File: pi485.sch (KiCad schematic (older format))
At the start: 25 parts, among them J1 RS485, P1 Rasperry Pi, P2 PWR, P3 Term, Q1 2N2222, Q2 2N2222, Q3 2N2222, U1 NE555, U2 MAX485

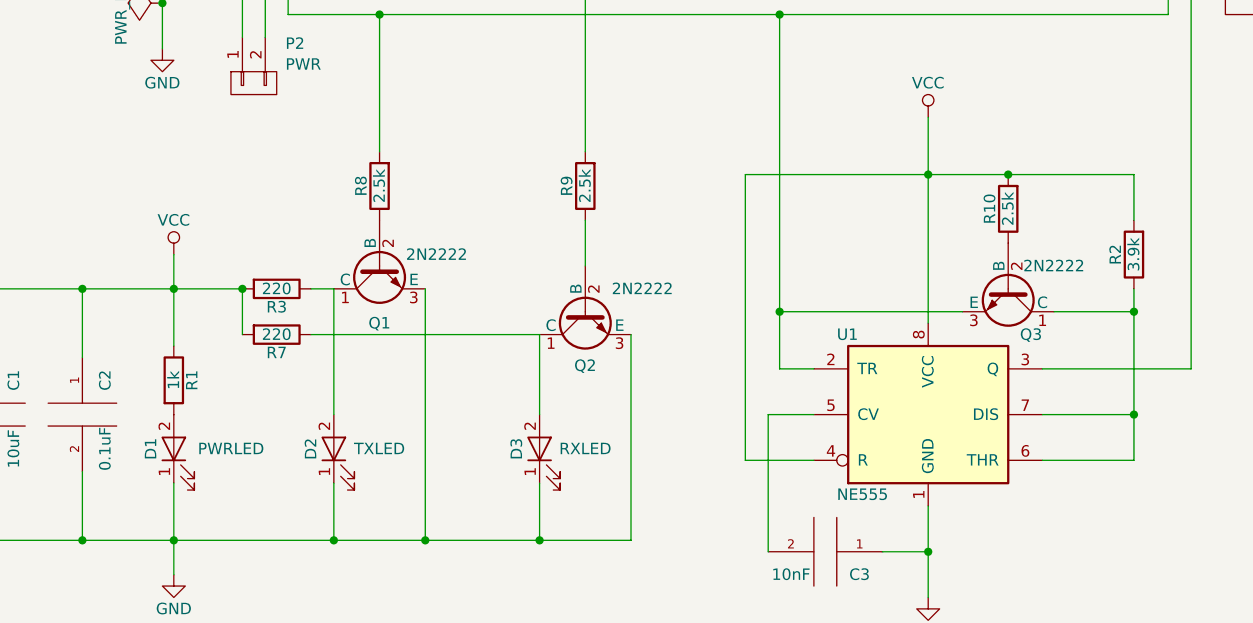
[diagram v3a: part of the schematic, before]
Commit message: Resistor / LED adjustments, BAT43 restoration (digi-key order placed). Footprint updates.
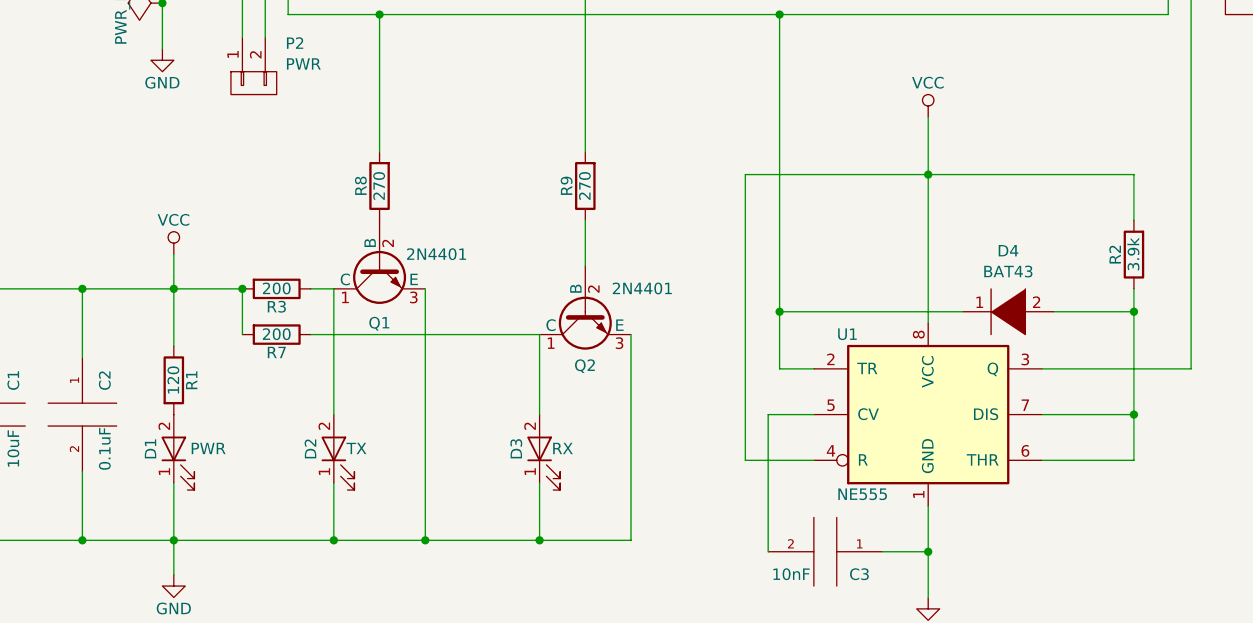
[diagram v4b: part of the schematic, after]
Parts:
- removed Q3: 2N2222, TO_SOT_Packages_THT:TO-92_Inline_Wide, symbol BC413
- removed R10: 2.5k, Resistors_THT:Resistor_Horizontal_RM7mm, symbol R
- added D4: BAT43, Diodes_THT:Diode_DO-35_SOD27_Horizontal_RM10, symbol DIODE
- C1: footprint Capacitors_THT:C_Rect_L7_W2.5_P5 -> Capacitors_THT:C_Radial_D5_L11_P2
- D1: value PWRLED -> PWR; footprint LEDs:LED-5MM -> LEDs:LED-3MM
- D2: value TXLED -> TX; footprint LEDs:LED-5MM -> LEDs:LED-3MM
- D3: value RXLED -> RX; footprint LEDs:LED-5MM -> LEDs:LED-3MM
- Q1, Q2: value 2N2222 -> 2N4401
- R1: value 1k -> 120
- R3, R7: value 220 -> 200
- R8, R9: value 2.5k -> 270
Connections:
- net (TXDO)_GPIO14: now also D4.1 (K)
- net at R2.1, U1.6 (THR), U1.7 (DIS): now also D4.2 (A)
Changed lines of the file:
@@
 Comp "Bryan Varner"
 Comment1 ""
-Comment2 ""
+Comment2 "Size resistor values R1, R3, and R7 appropriately for your LED choices."
 Comment3 "Implements half-duplex with TX latched RE/DE"
 Comment4 "Raspberry Pi / Arduino UART to RS485"
 $EndDescr
 $Comp
-L GND #PWR01
+L GND #PWR2
 U 1 1 586E82C6
 P 2150 3250
-F 0 "#PWR01" H 2150 3000 50  0001 C CNN
+F 0 "#PWR2" H 2150 3000 50  0001 C CNN
 F 1 "GND" H 2150 3100 50  0000 C CNN
 F 2 "" H 2150 3250 50  0000 C CNN
@@
 $EndComp
 $Comp
-L PWR_FLAG #FLG02
+L PWR_FLAG #FLG1
 U 1 1 586E8329
 P 2150 2150
-F 0 "#FLG02" H 2150 2245 50  0001 C CNN
+F 0 "#FLG1" H 2150 2245 50  0001 C CNN
 F 1 "PWR_FLAG" H 2150 2330 50  0000 C CNN
 F 2 "" H 2150 2150 50  0000 C CNN
@@
 $EndComp
 $Comp
-L PWR_FLAG #FLG03
+L PWR_FLAG #FLG2
 U 1 1 586E8340
 P 2150 3050
-F 0 "#FLG03" H 2150 3145 50  0001 C CNN
+F 0 "#FLG2" H 2150 3145 50  0001 C CNN
 F 1 "PWR_FLAG" H 2150 3230 50  0000 C CNN
 F 2 "" H 2150 3050 50  0000 C CNN
@@
 $EndComp
 $Comp
-L VCC #PWR04
+L VCC #PWR1
 U 1 1 586E83C6
 P 2150 1850
-F 0 "#PWR04" H 2150 1700 50  0001 C CNN
+F 0 "#PWR1" H 2150 1700 50  0001 C CNN
 F 1 "VCC" H 2150 2000 50  0000 C CNN
 F 2 "" H 2150 1850 50  0000 C CNN
@@
 $EndComp
 $Comp
-L VCC #PWR05
+L VCC #PWR3
 U 1 1 586E8496
 P 2200 4150
-F 0 "#PWR05" H 2200 4000 50  0001 C CNN
+F 0 "#PWR3" H 2200 4000 50  0001 C CNN
 F 1 "VCC" H 2200 4300 50  0000 C CNN
 F 2 "" H 2200 4150 50  0000 C CNN
@@
 $EndComp
 $Comp
-L GND #PWR06
+L GND #PWR4
 U 1 1 586E84AD
 P 2200 5550
-F 0 "#PWR06" H 2200 5300 50  0001 C CNN
+F 0 "#PWR4" H 2200 5300 50  0001 C CNN
 F 1 "GND" H 2200 5400 50  0000 C CNN
 F 2 "" H 2200 5550 50  0000 C CNN
@@
 P 2200 4700
 F 0 "R1" V 2280 4700 50  0000 C CNN
-F 1 "1k" V 2200 4700 50  0000 C CNN
+F 1 "120" V 2200 4700 50  0000 C CNN
 F 2 "Resistors_THT:Resistor_Horizontal_RM7mm" V 2350 4000 50  0001 C CNN
 F 3 "" H 2200 4700 50  0000 C CNN
@@
 P 2200 5000
 F 0 "D1" H 2200 5100 50  0000 C CNN
-F 1 "PWRLED" V 2200 4750 50  0000 C CNN
-F 2 "LEDs:LED-5MM" H 2150 4800 50  0001 C CNN
+F 1 "PWR" V 2200 4850 50  0000 C CNN
+F 2 "LEDs:LED-3MM" H 2150 4800 50  0001 C CNN
 F 3 "" H 2200 5000 50  0000 C CNN
 	1    2200 5000
@@
 $EndComp
 $Comp
-L GND #PWR07
+L GND #PWR6
 U 1 1 586E98F0
 P 5500 5650
-F 0 "#PWR07" H 5500 5400 50  0001 C CNN
+F 0 "#PWR6" H 5500 5400 50  0001 C CNN
 F 1 "GND" H 5500 5500 50  0000 C CNN
 F 2 "" H 5500 5650 50  0000 C CNN
@@
 $EndComp
 $Comp
-L VCC #PWR08
+L VCC #PWR5
 U 1 1 586E9922
 P 5500 3550
-F 0 "#PWR08" H 5500 3400 50  0001 C CNN
+F 0 "#PWR5" H 5500 3400 50  0001 C CNN
 F 1 "VCC" H 5500 3700 50  0000 C CNN
 F 2 "" H 5500 3550 50  0000 C CNN
@@
 $EndComp
 $Comp
-L GND #PWR09
+L GND #PWR8
 U 1 1 586EB44F
 P 7100 3500
-F 0 "#PWR09" H 7100 3250 50  0001 C CNN
+F 0 "#PWR8" H 7100 3250 50  0001 C CNN
 F 1 "GND" H 7100 3350 50  0000 C CNN
 F 2 "" H 7100 3500 50  0000 C CNN
@@
 $EndComp
 $Comp
-L VCC #PWR010
+L VCC #PWR7
 U 1 1 586EB484
 P 7100 1650
-F 0 "#PWR010" H 7100 1500 50  0001 C CNN
+F 0 "#PWR7" H 7100 1500 50  0001 C CNN
 F 1 "VCC" H 7100 1800 50  0000 C CNN
 F 2 "" H 7100 1650 50  0000 C CNN
@@
 GND
 $Comp
-L GND #PWR011
+L GND #PWR9
 U 1 1 586F0172
 P 8250 1900
-F 0 "#PWR011" H 8250 1650 50  0001 C CNN
+F 0 "#PWR9" H 8250 1650 50  0001 C CNN
 F 1 "GND" H 8250 1750 50  0000 C CNN
 F 2 "" H 8250 1900 50  0000 C CNN
@@
 $EndComp
 $Comp
-L VCC #PWR012
+L VCC #PWR10
 U 1 1 586F01EA
 P 8250 3300
-F 0 "#PWR012" H 8250 3150 50  0001 C CNN
+F 0 "#PWR10" H 8250 3150 50  0001 C CNN
 F 1 "VCC" H 8250 3450 50  0000 C CNN
 F 2 "" H 8250 3300 50  0000 C CNN
@@
 $EndComp
 $Comp
-L R R10
-U 1 1 5876AB08
-P 5850 3950
-F 0 "R10" V 5930 3950 50  0000 C CNN
-F 1 "2.5k" V 5850 3950 50  0000 C CNN
-F 2 "Resistors_THT:Resistor_Horizontal_RM7mm" H 4950 3950 50  0001 C CNN
-F 3 "" H 5850 3950 50  0000 C CNN
-	1    5850 3950
-	-1   0    0    1
-$EndComp
-$Comp
-L BC413 Q3
-U 1 1 5876AECB
-P 5850 4300
-F 0 "Q3" V 6050 4400 50  0000 C CNN
-F 1 "2N2222" V 5750 4500 50  0000 C CNN
-F 2 "TO_SOT_Packages_THT:TO-92_Inline_Wide" V 6268 4300 50  0001 C CIN
-F 3 "" H 5850 4300 50  0000 L CNN
-	1    5850 4300
-	0    1    1    0
-$EndComp
-$Comp
 L BC413 Q1
 U 1 1 5876C3F8
 P 3100 4200
 F 0 "Q1" V 3350 4200 50  0000 C CNN
-F 1 "2N2222" V 3050 3950 50  0000 C CNN
+F 1 "2N4401" V 3050 3950 50  0000 C CNN
 F 2 "TO_SOT_Packages_THT:TO-92_Inline_Wide" V 3518 4200 50  0001 C CIN
 F 3 "" H 3100 4200 50  0000 L CNN
@@
 P 4000 4400
 F 0 "Q2" V 4236 4400 50  0000 C CNN
-F 1 "2N2222" V 3900 4150 50  0000 C CNN
+F 1 "2N4401" V 3900 4150 50  0000 C CNN
 F 2 "TO_SOT_Packages_THT:TO-92_Inline_Wide" V 4418 4400 50  0001 C CIN
 F 3 "" H 4000 4400 50  0000 L CNN
@@
 P 2900 5000
 F 0 "D2" H 2900 5100 50  0000 C CNN
-F 1 "TXLED" V 2900 4800 50  0000 C CNN
-F 2 "LEDs:LED-5MM" H 2850 4800 50  0001 C CNN
+F 1 "TX" V 2900 4900 50  0000 C CNN
+F 2 "LEDs:LED-3MM" H 2850 4800 50  0001 C CNN
 F 3 "" H 2900 5000 50  0000 C CNN
 	1    2900 5000
@@
 P 3800 5000
 F 0 "D3" H 3800 5100 50  0000 C CNN
-F 1 "RXLED" V 3800 4800 50  0000 C CNN
-F 2 "LEDs:LED-5MM" H 3750 4800 50  0001 C CNN
+F 1 "RX" V 3800 4900 50  0000 C CNN
+F 2 "LEDs:LED-3MM" H 3750 4800 50  0001 C CNN
 F 3 "" H 3800 5000 50  0000 C CNN
 	1    3800 5000
@@
 P 2650 4500
 F 0 "R7" V 2730 4500 50  0000 C CNN
-F 1 "220" V 2650 4500 50  0000 C CNN
+F 1 "200" V 2650 4500 50  0000 C CNN
 F 2 "Resistors_THT:Resistor_Horizontal_RM7mm" V 2800 3800 50  0001 C CNN
 F 3 "" H 2650 4500 50  0000 C CNN
@@
 P 2650 4300
 F 0 "R3" V 2730 4300 50  0000 C CNN
-F 1 "220" V 2650 4300 50  0000 C CNN
+F 1 "200" V 2650 4300 50  0000 C CNN
 F 2 "Resistors_THT:Resistor_Horizontal_RM7mm" V 2800 3600 50  0001 C CNN
 F 3 "" H 2650 4300 50  0000 C CNN
@@
 P 3100 3850
 F 0 "R8" V 3180 3850 50  0000 C CNN
-F 1 "2.5k" V 3100 3850 50  0000 C CNN
+F 1 "270" V 3100 3850 50  0000 C CNN
 F 2 "Resistors_THT:Resistor_Horizontal_RM15mm" V 3250 3150 50  0001 C CNN
 F 3 "" H 3100 3850 50  0000 C CNN
@@
 P 4000 3850
 F 0 "R9" V 4080 3850 50  0000 C CNN
-F 1 "2.5k" V 4000 3850 50  0000 C CNN
+F 1 "270" V 4000 3850 50  0000 C CNN
 F 2 "Resistors_THT:Resistor_Horizontal_RM7mm" V 4150 3150 50  0001 C CNN
 F 3 "" H 4000 3850 50  0000 C CNN
@@
 F 0 "C1" V 1500 5000 50  0000 C CNN
 F 1 "10uF" V 1500 4700 50  0000 C CNN
-F 2 "Capacitors_THT:C_Rect_L7_W2.5_P5" V 1600 4550 50  0001 C CNN
+F 2 "Capacitors_THT:C_Radial_D5_L11_P2" V 1600 4550 50  0001 C CNN
 F 3 "" H 1400 4850 50  0000 C CNN
 	1    1400 4850
@@
 	1800 4600 1800 4300
 Connection ~ 1800 4300
-Connection ~ 5850 3800
 Wire Wire Line
 	6050 4400 6400 4400
+$Comp
+L DIODE D4
+U 1 1 5879650D
+P 5850 4400
+F 0 "D4" H 5850 4665 50  0000 C CNN
+F 1 "BAT43" H 5850 4574 50  0000 C CNN
+F 2 "Diodes_THT:Diode_DO-35_SOD27_Horizontal_RM10" H 5850 4573 50  0001 C CNN
+F 3 "" H 5850 4400 50  0000 C CNN
+	1    5850 4400
+	1    0    0    -1
+$EndComp
 $EndSCHEMATC

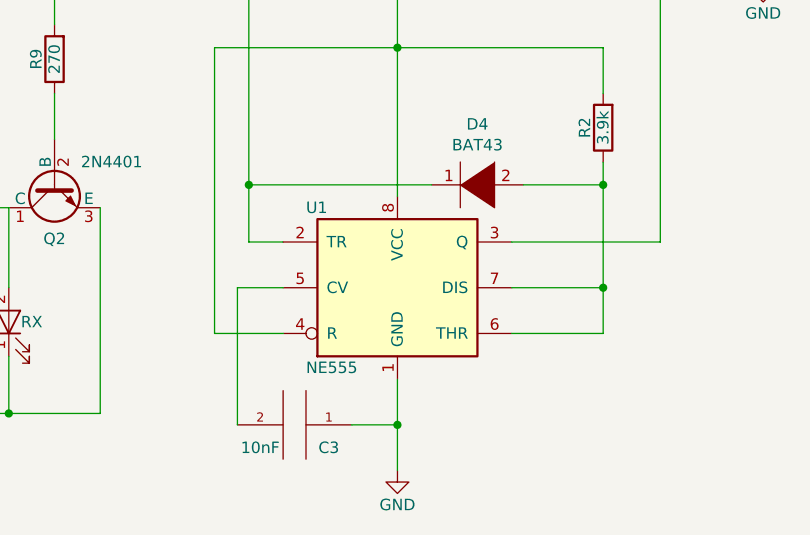
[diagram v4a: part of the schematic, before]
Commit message: * Rotated board 90 degrees. * Major update to footprints. Resistors are 10mm, LEDs are 3mm. * Manually re-routed / cleaned up traces & positiiong of quite a few things. * This could be pulled so much tighter, but to keep it 'simple soldering' I'm deliberately keeping big honkin traces with lots of clearance. * Fixed a major issue where I had accidentally forgotten the discharge capacitor by deleting the wrong one. The CTRL pin of the 555 should be jumperable to GND to keep the output of the 555 low, regardless of input (latch disable).
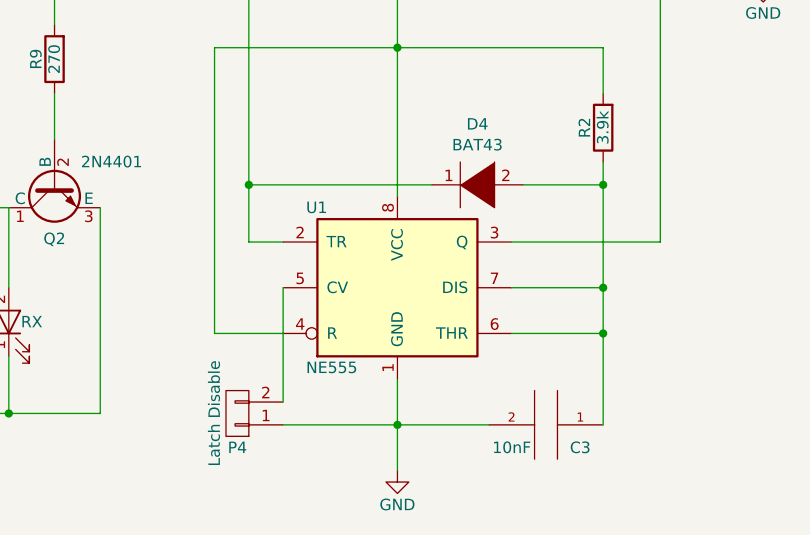
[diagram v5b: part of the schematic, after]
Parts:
- added P4: Latch Disable, Pin_Headers:Pin_Header_Straight_1x02, symbol CONN_01X02
- R1, R3, R4, R5, R6, R7, R9: footprint Resistors_THT:Resistor_Horizontal_RM7mm -> Resistors_THT:Resistor_Horizontal_RM10mm
- R8: footprint Resistors_THT:Resistor_Horizontal_RM15mm -> Resistors_THT:Resistor_Horizontal_RM10mm
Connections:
- net GND: now also C3.2, P4.1 (P1); no longer C3.1
- net at U1.5 (CV): now also P4.2 (P2); no longer C3.2
- net at D4.2 (A), R2.1, U1.6 (THR)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: now also C3.1
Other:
- moved on the sheet: C3
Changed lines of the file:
@@
 Title "Pi485"
 Date "2017-01-12"
-Rev "1.0.1"
+Rev "1.0.4"
 Comp "Bryan Varner"
 Comment1 ""
@@
 $EndDescr
 $Comp
-L GND #PWR2
+L GND #PWR01
 U 1 1 586E82C6
 P 2150 3250
-F 0 "#PWR2" H 2150 3000 50  0001 C CNN
+F 0 "#PWR01" H 2150 3000 50  0001 C CNN
 F 1 "GND" H 2150 3100 50  0000 C CNN
 F 2 "" H 2150 3250 50  0000 C CNN
@@
 $EndComp
 $Comp
-L PWR_FLAG #FLG1
+L PWR_FLAG #FLG02
 U 1 1 586E8329
 P 2150 2150
-F 0 "#FLG1" H 2150 2245 50  0001 C CNN
+F 0 "#FLG02" H 2150 2245 50  0001 C CNN
 F 1 "PWR_FLAG" H 2150 2330 50  0000 C CNN
 F 2 "" H 2150 2150 50  0000 C CNN
@@
 $EndComp
 $Comp
-L PWR_FLAG #FLG2
+L PWR_FLAG #FLG03
 U 1 1 586E8340
 P 2150 3050
-F 0 "#FLG2" H 2150 3145 50  0001 C CNN
+F 0 "#FLG03" H 2150 3145 50  0001 C CNN
 F 1 "PWR_FLAG" H 2150 3230 50  0000 C CNN
 F 2 "" H 2150 3050 50  0000 C CNN
@@
 $EndComp
 $Comp
-L VCC #PWR1
+L VCC #PWR04
 U 1 1 586E83C6
 P 2150 1850
-F 0 "#PWR1" H 2150 1700 50  0001 C CNN
+F 0 "#PWR04" H 2150 1700 50  0001 C CNN
 F 1 "VCC" H 2150 2000 50  0000 C CNN
 F 2 "" H 2150 1850 50  0000 C CNN
@@
 $EndComp
 $Comp
-L VCC #PWR3
+L VCC #PWR05
 U 1 1 586E8496
 P 2200 4150
-F 0 "#PWR3" H 2200 4000 50  0001 C CNN
+F 0 "#PWR05" H 2200 4000 50  0001 C CNN
 F 1 "VCC" H 2200 4300 50  0000 C CNN
 F 2 "" H 2200 4150 50  0000 C CNN
@@
 $EndComp
 $Comp
-L GND #PWR4
+L GND #PWR06
 U 1 1 586E84AD
 P 2200 5550
-F 0 "#PWR4" H 2200 5300 50  0001 C CNN
+F 0 "#PWR06" H 2200 5300 50  0001 C CNN
 F 1 "GND" H 2200 5400 50  0000 C CNN
 F 2 "" H 2200 5550 50  0000 C CNN
@@
 F 0 "R1" V 2280 4700 50  0000 C CNN
 F 1 "120" V 2200 4700 50  0000 C CNN
-F 2 "Resistors_THT:Resistor_Horizontal_RM7mm" V 2350 4000 50  0001 C CNN
+F 2 "Resistors_THT:Resistor_Horizontal_RM10mm" V 2350 4000 50  0001 C CNN
 F 3 "" H 2200 4700 50  0000 C CNN
 	1    2200 4700
@@
 L CAP C3
 U 1 1 586E89BC
-P 5050 5450
-F 0 "C3" V 5150 5600 50  0000 C CNN
-F 1 "10nF" V 5150 5300 50  0000 C CNN
-F 2 "Capacitors_THT:C_Rect_L7_W2.5_P5" V 5250 5150 50  0001 C CNN
-F 3 "" H 5050 5450 50  0000 C CNN
-	1    5050 5450
+P 6150 5450
+F 0 "C3" V 6250 5600 50  0000 C CNN
+F 1 "10nF" V 6250 5300 50  0000 C CNN
+F 2 "Capacitors_THT:C_Rect_L7_W2.5_P5" V 6350 5150 50  0001 C CNN
+F 3 "" H 6150 5450 50  0000 C CNN
+	1    6150 5450
 	0    1    1    0
 $EndComp
 $Comp
-L GND #PWR6
+L GND #PWR07
 U 1 1 586E98F0
 P 5500 5650
-F 0 "#PWR6" H 5500 5400 50  0001 C CNN
+F 0 "#PWR07" H 5500 5400 50  0001 C CNN
 F 1 "GND" H 5500 5500 50  0000 C CNN
 F 2 "" H 5500 5650 50  0000 C CNN
@@
 $EndComp
 $Comp
-L VCC #PWR5
+L VCC #PWR08
 U 1 1 586E9922
 P 5500 3550
-F 0 "#PWR5" H 5500 3400 50  0001 C CNN
+F 0 "#PWR08" H 5500 3400 50  0001 C CNN
 F 1 "VCC" H 5500 3700 50  0000 C CNN
 F 2 "" H 5500 3550 50  0000 C CNN
@@
 $EndComp
 $Comp
-L GND #PWR8
+L GND #PWR09
 U 1 1 586EB44F
 P 7100 3500
-F 0 "#PWR8" H 7100 3250 50  0001 C CNN
+F 0 "#PWR09" H 7100 3250 50  0001 C CNN
 F 1 "GND" H 7100 3350 50  0000 C CNN
 F 2 "" H 7100 3500 50  0000 C CNN
@@
 $EndComp
 $Comp
-L VCC #PWR7
+L VCC #PWR010
 U 1 1 586EB484
 P 7100 1650
-F 0 "#PWR7" H 7100 1500 50  0001 C CNN
+F 0 "#PWR010" H 7100 1500 50  0001 C CNN
 F 1 "VCC" H 7100 1800 50  0000 C CNN
 F 2 "" H 7100 1650 50  0000 C CNN
@@
 F 0 "R5" V 8080 2450 50  0000 C CNN
 F 1 "120" V 8000 2450 50  0000 C CNN
-F 2 "Resistors_THT:Resistor_Horizontal_RM7mm" H 8850 2650 50  0001 C CNN
+F 2 "Resistors_THT:Resistor_Horizontal_RM10mm" H 8850 2650 50  0001 C CNN
 F 3 "" H 8000 2450 50  0000 C CNN
 	1    8000 2450
@@
 F 0 "R4" V 8080 2050 50  0000 C CNN
 F 1 "20k" V 8000 2050 50  0000 C CNN
-F 2 "Resistors_THT:Resistor_Horizontal_RM7mm" H 8850 2300 50  0001 C CNN
+F 2 "Resistors_THT:Resistor_Horizontal_RM10mm" H 8850 2300 50  0001 C CNN
 F 3 "" H 8000 2050 50  0000 C CNN
 	1    8000 2050
@@
 F 0 "R6" V 8080 3150 50  0000 C CNN
 F 1 "20k" V 8000 3150 50  0000 C CNN
-F 2 "Resistors_THT:Resistor_Horizontal_RM7mm" H 8850 3300 50  0001 C CNN
+F 2 "Resistors_THT:Resistor_Horizontal_RM10mm" H 8850 3300 50  0001 C CNN
 F 3 "" H 8000 3150 50  0000 C CNN
 	1    8000 3150
@@
 GND
 $Comp
-L GND #PWR9
+L GND #PWR011
 U 1 1 586F0172
 P 8250 1900
-F 0 "#PWR9" H 8250 1650 50  0001 C CNN
+F 0 "#PWR011" H 8250 1650 50  0001 C CNN
 F 1 "GND" H 8250 1750 50  0000 C CNN
 F 2 "" H 8250 1900 50  0000 C CNN
@@
 $EndComp
 $Comp
-L VCC #PWR10
+L VCC #PWR012
 U 1 1 586F01EA
 P 8250 3300
-F 0 "#PWR10" H 8250 3150 50  0001 C CNN
+F 0 "#PWR012" H 8250 3150 50  0001 C CNN
 F 1 "VCC" H 8250 3450 50  0000 C CNN
 F 2 "" H 8250 3300 50  0000 C CNN
@@
 F 0 "R7" V 2730 4500 50  0000 C CNN
 F 1 "200" V 2650 4500 50  0000 C CNN
-F 2 "Resistors_THT:Resistor_Horizontal_RM7mm" V 2800 3800 50  0001 C CNN
+F 2 "Resistors_THT:Resistor_Horizontal_RM10mm" V 2800 3800 50  0001 C CNN
 F 3 "" H 2650 4500 50  0000 C CNN
 	1    2650 4500
@@
 F 0 "R3" V 2730 4300 50  0000 C CNN
 F 1 "200" V 2650 4300 50  0000 C CNN
-F 2 "Resistors_THT:Resistor_Horizontal_RM7mm" V 2800 3600 50  0001 C CNN
+F 2 "Resistors_THT:Resistor_Horizontal_RM10mm" V 2800 3600 50  0001 C CNN
 F 3 "" H 2650 4300 50  0000 C CNN
 	1    2650 4300
@@
 F 0 "R8" V 3180 3850 50  0000 C CNN
 F 1 "270" V 3100 3850 50  0000 C CNN
-F 2 "Resistors_THT:Resistor_Horizontal_RM15mm" V 3250 3150 50  0001 C CNN
+F 2 "Resistors_THT:Resistor_Horizontal_RM10mm" V 3250 3150 50  0001 C CNN
 F 3 "" H 3100 3850 50  0000 C CNN
 	1    3100 3850
@@
 F 0 "R9" V 4080 3850 50  0000 C CNN
 F 1 "270" V 4000 3850 50  0000 C CNN
-F 2 "Resistors_THT:Resistor_Horizontal_RM7mm" V 4150 3150 50  0001 C CNN
+F 2 "Resistors_THT:Resistor_Horizontal_RM10mm" V 4150 3150 50  0001 C CNN
 F 3 "" H 4000 3850 50  0000 C CNN
 	1    4000 3850
@@
 	5500 3550 5500 4450
 Wire Wire Line
-	6400 4300 6400 5050
+	6400 4300 6400 5450
 Wire Wire Line
 	6400 4850 6000 4850
@@
 Connection ~ 6400 4850
 Wire Wire Line
-	5300 5450 5500 5450
+	5000 5450 5900 5450
 Wire Wire Line
 	5500 5250 5500 5650
 Connection ~ 5500 5450
-Wire Wire Line
-	5000 4850 4800 4850
-Wire Wire Line
-	4800 4850 4800 5450
 Wire Wire Line
 	5000 5050 4700 5050
@@
 	1    0    0    -1
 $EndComp
+Connection ~ 6400 5050
+$Comp
+L CONN_01X02 P4
+U 1 1 587D51D9
+P 4800 5400
+F 0 "P4" H 4800 5550 50  0000 C CNN
+F 1 "Latch Disable" V 4900 5400 50  0000 C CNN
+F 2 "Pin_Headers:Pin_Header_Straight_1x02" H 5450 5650 50  0001 C CNN
+F 3 "" H 4800 5400 50  0000 C CNN
+	1    4800 5400
+	-1   0    0    1
+$EndComp
+Wire Wire Line
+	5000 5350 5000 4850
 $EndSCHEMATC

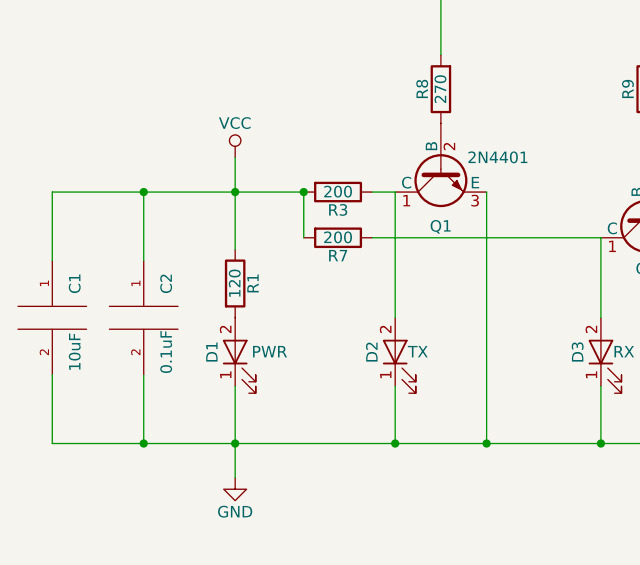
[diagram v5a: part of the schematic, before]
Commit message: Fixed the footprint issues with the 2N4401 transistors being 'backwards'
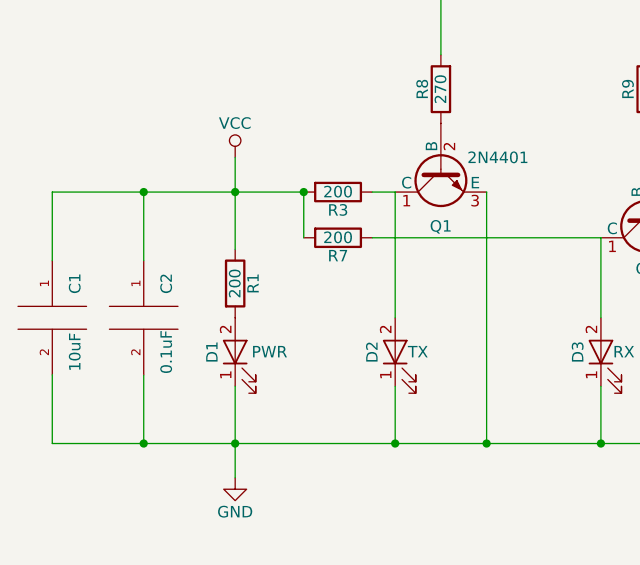
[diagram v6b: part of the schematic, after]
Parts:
- R1: value 120 -> 200
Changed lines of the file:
@@
 P 2200 4700
 F 0 "R1" V 2280 4700 50  0000 C CNN
-F 1 "120" V 2200 4700 50  0000 C CNN
+F 1 "200" V 2200 4700 50  0000 C CNN
 F 2 "Resistors_THT:Resistor_Horizontal_RM10mm" V 2350 4000 50  0001 C CNN
 F 3 "" H 2200 4700 50  0000 C CNN

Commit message: 1.1.0 bump. Added 3.3v control pin to turn on power to the 485 and the PWR LED.
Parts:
- added Q3: 2N4401, TO_SOT_Packages_THT:TO-92_Inline_Wide, symbol BC413
- added R10: 270, Resistors_THT:Resistor_Horizontal_RM10mm, symbol R
- P1: footprint Socket_Strips:Socket_Strip_Angled_1x04 -> Socket_Strips:Socket_Strip_Angled_1x05; symbol CONN_01X04 -> CONN_01X05
- R2: footprint Resistors_THT:Resistor_Horizontal_RM7mm -> Resistors_THT:Resistor_Horizontal_RM10mm
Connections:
- net VCC: now also Q3.1 (C); no longer R1.1, U2.8 (VDD)
- new net: Q3.3 (E), R1.1, U2.8 (VDD)
- new net: Q3.2 (B), R10.1
- new net (485PWR)_GPIO18: P1.5 (P5), R10.2
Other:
- moved on the sheet: C1, C2, D1, R1
